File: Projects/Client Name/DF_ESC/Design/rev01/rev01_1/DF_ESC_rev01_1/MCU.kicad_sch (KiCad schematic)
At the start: 38 parts, among them U1 STM32F405RGTx

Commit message: update 2024-02-27
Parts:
- renumbered U1 to U?

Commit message: Update 2024-02-28_2
Input Proteccion Done
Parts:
- renumbered C1 to C?, R2 to R?, R1 to R?, R3 to R?

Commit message: Update 2024-02-03
Schematic finish but DRC CHEK Errors
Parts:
- removed J?: Conn_01x03_Pin, symbol Connector:Conn_01x03_Pin
- removed J?: Conn_01x08_Pin, symbol Connector:Conn_01x08_Pin
- removed J?: Conn_01x06_Pin, symbol Connector:Conn_01x06_Pin
- added J2: HX25003-8AWB, DF_ESC_Footprint_Library:CONN-SMD_8P-P2.50_HX25003-8AWB, symbol DF_ESC_Symbol_Library_Casa:HX25003-8AWB
- added J7: S6B-XH-SM4-TB(LF)(SN), DF_ESC_Footprint_Library_Casa:CONN-SMD_S6B-XH-SM4-TB-LF-SN, symbol DF_ESC_Symbol_Library_Casa:S6B-XH-SM4-TB(LF)(SN)
- added J8: XH-3AWB, DF_ESC_Footprint_Library_Casa:CONN-SMD_XH-3AWB, symbol DF_ESC_Symbol_Library_Casa:XH-3AWB
- C10, C11, C12, C13, C14, C15, C16, C17, C18, C19, C20, C21, C22, C23, C24, C25, C9: renamed from C?; footprint (none) -> Capacitor_SMD:C_0603_1608Metric_Pad1.08x0.95mm_HandSolder
- D6, D7, D8: renamed from D?; footprint (none) -> LED_SMD:LED_1206_3216Metric_Pad1.42x1.75mm_HandSolder
- FB1: renamed from FB?; footprint (none) -> Inductor_SMD:L_0603_1608Metric_Pad1.05x0.95mm_HandSolder
- R10, R11, R12, R13, R14, R15, R16, R7, R8, R9: renamed from R?; footprint (none) -> Resistor_SMD:R_0603_1608Metric_Pad0.98x0.95mm_HandSolder
- SW1: renamed from SW?; footprint (none) -> DF_ESC_Footprint_Library_Casa:SW-SMD_4P-L5.2-W5.2-P3.70-LS6.4
- TH2: renamed from TH?; footprint (none) -> Resistor_SMD:R_0603_1608Metric_Pad0.98x0.95mm_HandSolder
- Y1: renamed from Y?; footprint (none) -> DF_ESC_Footprint_Library_Casa:CRYSTAL-SMD_L5.0-W3.2
- gave numbers to parts that had none: 1
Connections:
- net +3V3: now also J2.2, J7.1
- net +5V: now also J2.1, J8.1
- net GND: now also J2.3, J2.8, J7.3, J8.2
- net MISO_ADC_EXT2: now also J2.7
- net RX_SCL_MOSI: now also J2.6
- net SCK_ADC_EXT: now also J2.4
- net SWCLK: now also J7.2, J7.4, J7.5
- net TX_SDA_NSS: now also J2.5
- net at R16.2: now also J8.3
- no-connect marks 18 -> 24
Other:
- note added: "[4] - MCU"
- note removed: "[3] - MCU"

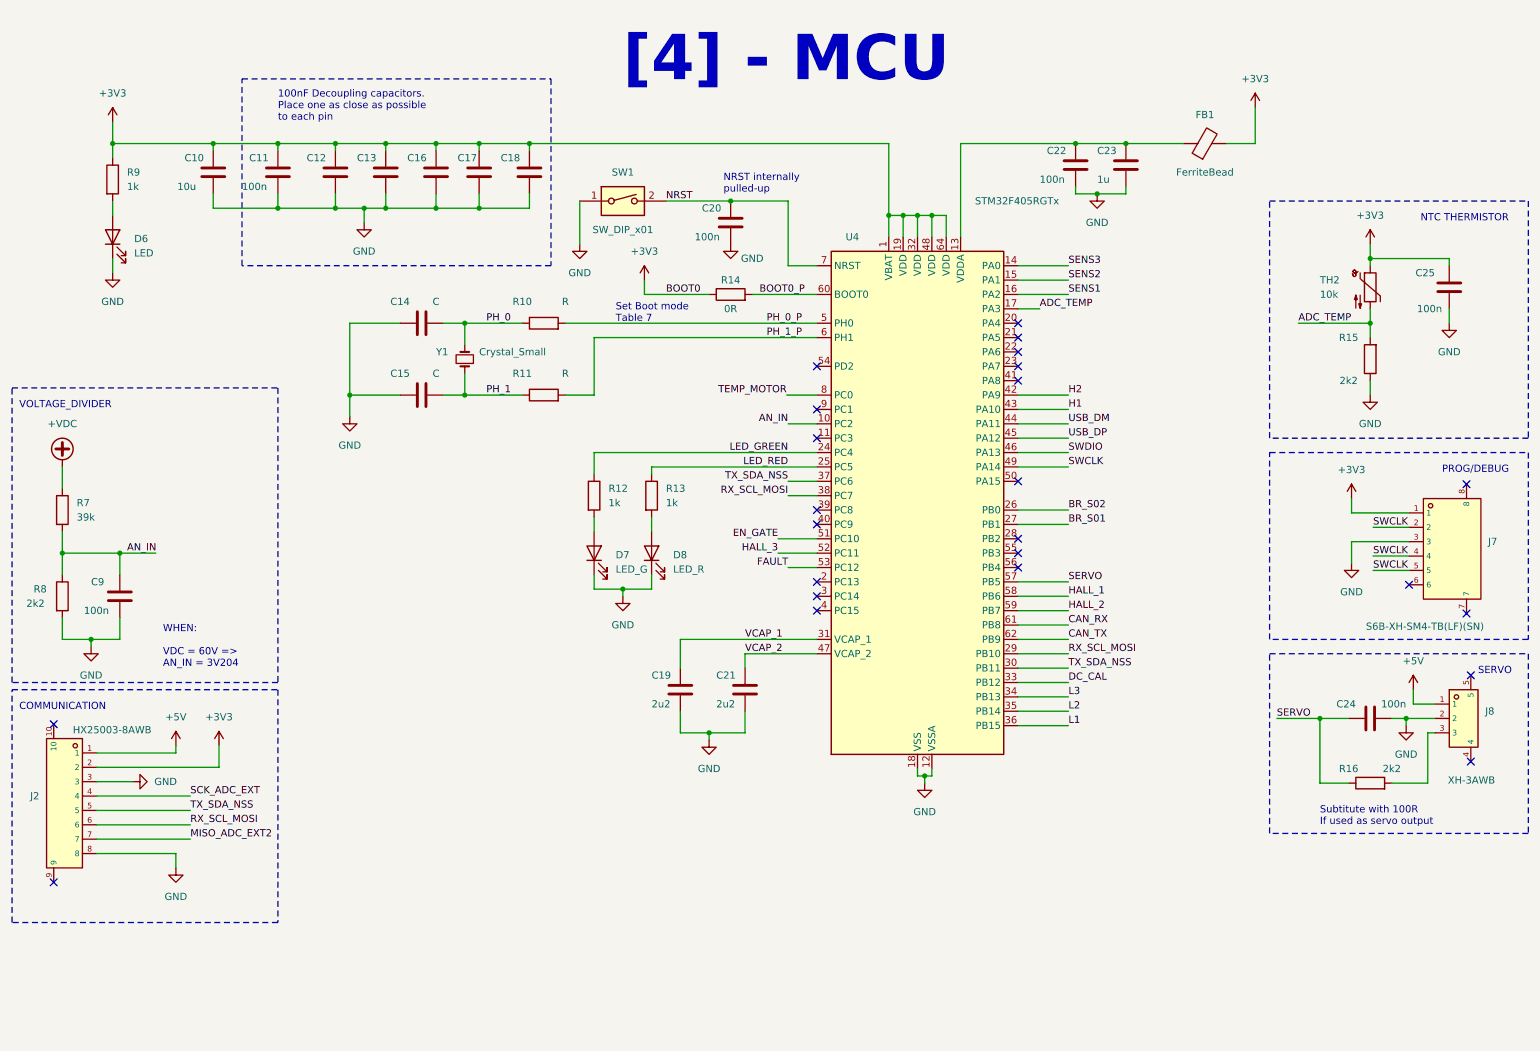
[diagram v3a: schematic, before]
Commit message: Update 2024-03-03
ERC 0 Errors. Update PCB from schematics prepare to going on
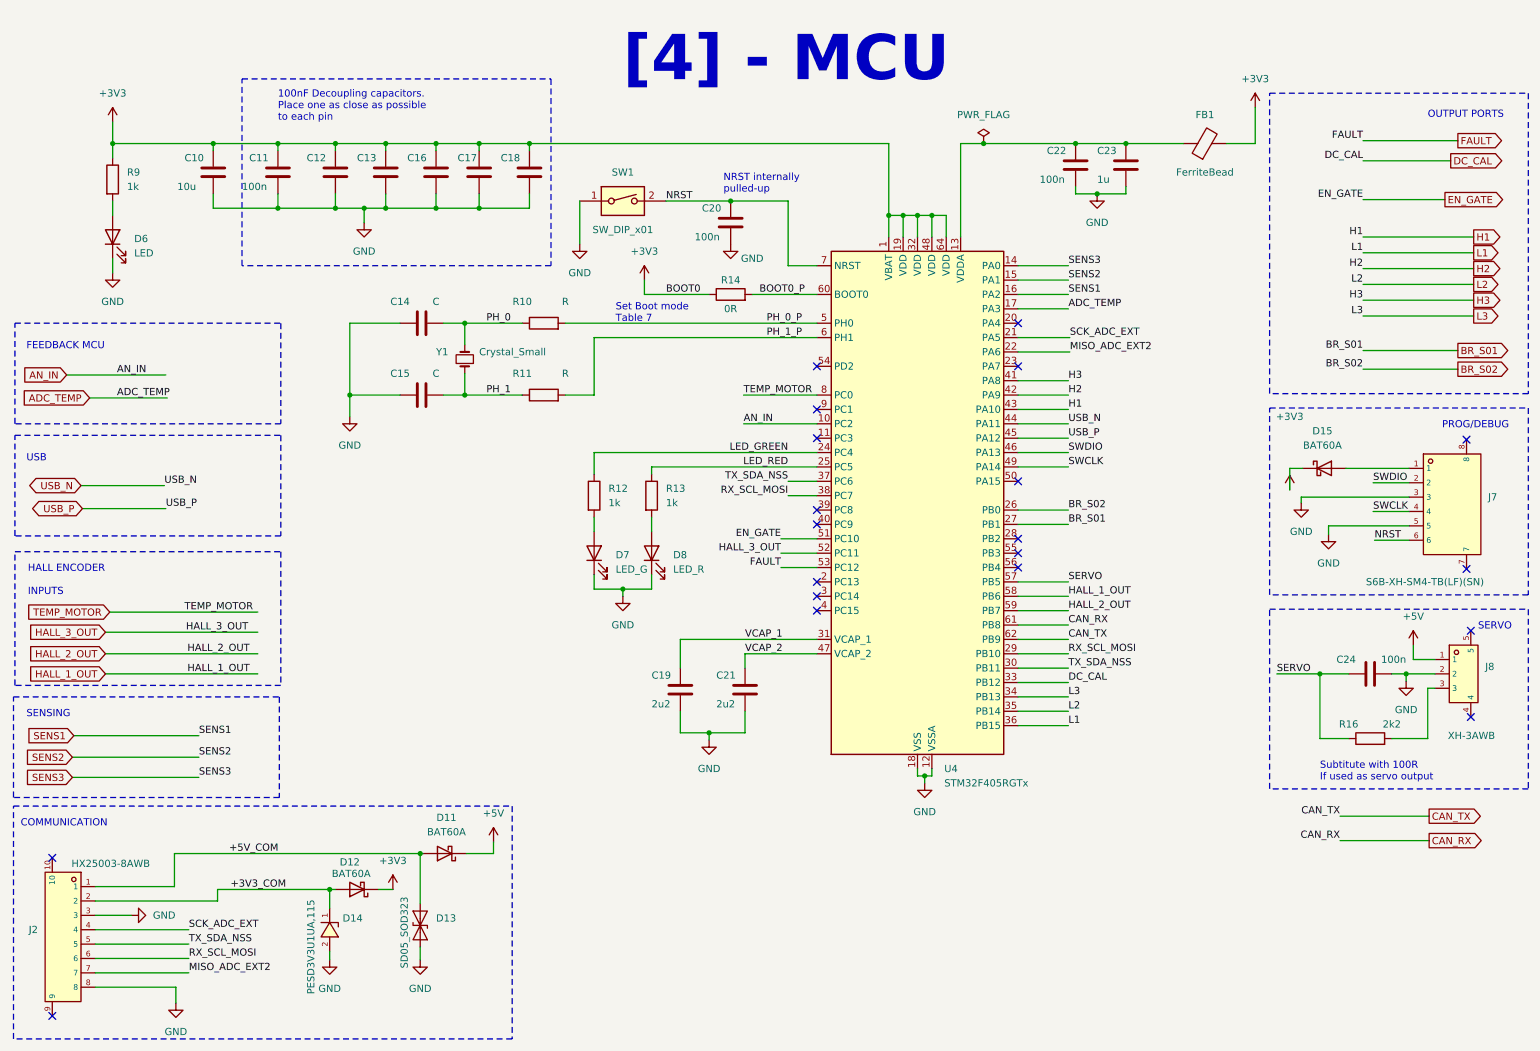
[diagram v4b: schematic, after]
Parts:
- removed C25, C9: 100n, Capacitor_SMD:C_0603_1608Metric_Pad1.08x0.95mm_HandSolder, symbol Device:C
- removed R15, R8: 2k2, Resistor_SMD:R_0603_1608Metric_Pad0.98x0.95mm_HandSolder, symbol Device:R
- removed R7: 39k, Resistor_SMD:R_0603_1608Metric_Pad0.98x0.95mm_HandSolder, symbol Device:R
- removed TH2: 10k, Resistor_SMD:R_0603_1608Metric_Pad0.98x0.95mm_HandSolder, symbol Device:Thermistor_NTC
- added D11, D12, D15: BAT60A, Diode_SMD:D_SOD-323, symbol Diode:BAT60A
- added D13: SD05_SOD323, Diode_SMD:D_SOD-323, symbol Diode:SD05_SOD323
- added D14: PESD3V3U1UA,115, PESD3V3U1UA:SOD-323_L1.7-W1.3-LS2.5-RD, symbol PESD3V3U1UA,115:PESD3V3U1UA,115
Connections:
- net +3V3: now also D12.1 (K), D15.1 (K); no longer J2.2, J7.1
- net +5V: now also D11.1 (K); no longer J2.1
- net GND: now also J7.5, D13.1 (A1), D14.2
- net MISO_ADC_EXT2: now also U4.22 (PA6)
- net NRST: now also J7.6
- net SCK_ADC_EXT: now also U4.21 (PA5)
- net SWCLK: no longer J7.2, J7.5
- net SWDIO: now also J7.2
- net H3: now reaches U4.41 (PA8)
- net HALL_1 renamed HALL_1_OUT
- net HALL_2 renamed HALL_2_OUT
- net HALL_3 renamed HALL_3_OUT
- net USB_DM renamed USB_N
- net USB_DP renamed USB_P
- new net: D15.2 (A), J7.1
- new net +3V3_COM: D12.2 (A), D14.1, J2.2
- new net +5V_COM: D11.2 (A), D13.2 (A2), J2.1
- no-connect marks 24 -> 20
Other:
- note added: "FEEDBACK MCU"
- note added: "HALL ENCODER INPUTS"
- note added: "OUTPUT PORTS"
- note added: "SENSING"
- note added: "USB"
- note removed: "NTC THERMISTOR"
- note removed: "VOLTAGE_DIVIDER"
- note removed: "WHEN: VDC = 60V => AN_IN = 3V204"
- moved on the sheet: C24, J2, J7, J8, R16

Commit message: Update 2024-03-03_2
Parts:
- renumbered C11 to C10, C12 to C11, C13 to C12, C14 to C13, C15 to C14, C16 to C15, C17 to C16, C18 to C17, C19 to C18, C20 to C19, C21 to C20, C22 to C21, C23 to C22, C24 to C23, C10 to C9, D11 to D10, D7 to D11, D8 to D12, D15 to D13, D14 to D7, D12 to D8, D13 to D9, J7 to J3, J8 to J4, R12 to R10, R13 to R11, R14 to R12, R16 to R13, R9 to R7, R10 to R8, R11 to R9, U4 to U3
